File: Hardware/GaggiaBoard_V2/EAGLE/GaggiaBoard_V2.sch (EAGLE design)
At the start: 113 parts, among them IC1 LD117AS33TR, J1 4PIN, J11 PIN262409-1, J12 PIN262409-1, J13 PIN262409-1, J14 PIN262409-1, J15 PIN262409-1, J16 PIN262409-1, J17 PIN262409-1, J18 PIN262409-1, J19 PIN262409-1, J2 Vertical Qwiic Connector, J20 PIN262409-1, J3 Vertical Qwiic Connector, J5 2PIN, J6 3PIN, J7 3PIN, J8 5PIN, J9 3PIN, K1 RELAY-SPDT-JZC-11F, K2 RELAY-SPDT-JZC-11F, K3 AQH213, Q1 600mA/40V, Q10 600mA/40V, Q11 MOSFET_PCH_DUAL-DMP2240UDM, Q2 600mA/40V, Q3 600mA/40V, Q4 600mA/40V, Q5 600mA/40V, Q6 600mA/40V, Q8 600mA/40V, Q9 600mA/40V, U1 BLACKPILL, U2 MAX31855K, U5 TXS0102

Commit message: snubbers
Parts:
- added C16: 10nF, rcl:C-USC1206
- added R35: 220, rcl:R-US_R2512
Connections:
- removed net N$32: C5.1, R13.2
- new net N$27: C5.2, R13.1
- new net N$31: C16.2, R35.1
- net 3WAY: now also R35.2
- net AC_N: no longer R13.1
- net AC_P: now also C16.1, C5.1
- net PUMP_P: now also R13.2; no longer C5.2
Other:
- moved on the sheet: C5, R13
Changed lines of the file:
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@@
 <attribute name="LCSC" value="C107696"/>
+</part>
+<part name="C16" library="rcl" library_urn="urn:adsk.eagle:library:334" deviceset="C-US" device="C1206" package3d_urn="urn:adsk.eagle:package:23618/2" value="10nF">
+<spice>
+<pinmapping spiceprefix="C">
+<pinmap gate="G$1" pin="1" pinorder="1"/>
+<pinmap gate="G$1" pin="2" pinorder="2"/>
+</pinmapping>
+</spice>
+<attribute name="LCSC" value="C107192"/>
+</part>
+<part name="R35" library="rcl" library_urn="urn:adsk.eagle:library:334" deviceset="R-US_" device="R2512" package3d_urn="urn:adsk.eagle:package:23545/2" value="220">
+<spice>
+<pinmapping spiceprefix="R">
+<pinmap gate="G$1" pin="1" pinorder="1"/>
+<pinmap gate="G$1" pin="2" pinorder="2"/>
+</pinmapping>
+</spice>
+<attribute name="LCSC" value="C877859"/>
 </part>
 </parts>
@@
 <instance part="MARK4" gate="G$1" x="243.84" y="40.64" smashed="yes"/>
 <instance part="MARK3" gate="G$1" x="241.3" y="40.64" smashed="yes"/>
-<instance part="R13" gate="G$1" x="205.74" y="165.1" smashed="yes">
-<attribute name="NAME" x="201.93" y="166.5986" size="1.778" layer="95"/>
-<attribute name="VALUE" x="201.93" y="161.798" size="1.778" layer="96"/>
-<attribute name="LCSC" x="205.74" y="165.1" size="1.778" layer="96" display="off"/>
-</instance>
-<instance part="C5" gate="G$1" x="215.9" y="165.1" smashed="yes" rot="R90">
-<attribute name="NAME" x="215.265" y="166.116" size="1.778" layer="95" rot="R90"/>
-<attribute name="VALUE" x="220.091" y="166.116" size="1.778" layer="96" rot="R90"/>
-<attribute name="LCSC" x="215.9" y="165.1" size="1.778" layer="96" rot="R90" display="off"/>
+<instance part="R13" gate="G$1" x="215.9" y="165.1" smashed="yes">
+<attribute name="NAME" x="212.09" y="166.5986" size="1.778" layer="95"/>
+<attribute name="VALUE" x="212.09" y="161.798" size="1.778" layer="96"/>
+<attribute name="LCSC" x="215.9" y="165.1" size="1.778" layer="96" display="off"/>
+</instance>
+<instance part="C5" gate="G$1" x="203.2" y="165.1" smashed="yes" rot="R90">
+<attribute name="NAME" x="202.565" y="166.116" size="1.778" layer="95" rot="R90"/>
+<attribute name="VALUE" x="207.391" y="166.116" size="1.778" layer="96" rot="R90"/>
+<attribute name="LCSC" x="203.2" y="165.1" size="1.778" layer="96" rot="R90" display="off"/>
 </instance>
 <instance part="Q8" gate="G$1" x="40.64" y="101.6" smashed="yes">
@@
 <attribute name="LCSC" x="185.42" y="137.16" size="1.778" layer="96" display="off"/>
 </instance>
+<instance part="C16" gate="G$1" x="203.2" y="147.32" smashed="yes" rot="R90">
+<attribute name="NAME" x="202.565" y="148.336" size="1.778" layer="95" rot="R90"/>
+<attribute name="VALUE" x="207.391" y="148.336" size="1.778" layer="96" rot="R90"/>
+<attribute name="LCSC" x="203.2" y="147.32" size="1.778" layer="96" rot="R90" display="off"/>
+</instance>
+<instance part="R35" gate="G$1" x="215.9" y="147.32" smashed="yes">
+<attribute name="NAME" x="212.09" y="148.8186" size="1.778" layer="95"/>
+<attribute name="VALUE" x="212.09" y="144.018" size="1.778" layer="96"/>
+<attribute name="LCSC" x="215.9" y="147.32" size="1.778" layer="96" display="off"/>
+</instance>
 </instances>
 <busses>
@@
 </segment>
 <segment>
-<label x="187.96" y="170.18" size="1.778" layer="95"/>
+<label x="210.82" y="170.18" size="1.778" layer="95"/>
 <pinref part="J18" gate="-1" pin="1"/>
-<pinref part="R13" gate="G$1" pin="1"/>
-<wire x1="198.12" y1="170.18" x2="226.06" y2="170.18" width="0.1524" layer="91"/>
-<wire x1="200.66" y1="165.1" x2="198.12" y2="165.1" width="0.1524" layer="91"/>
-<wire x1="198.12" y1="165.1" x2="198.12" y2="170.18" width="0.1524" layer="91"/>
-<junction x="198.12" y="170.18"/>
-<wire x1="187.96" y1="170.18" x2="198.12" y2="170.18" width="0.1524" layer="91"/>
+<wire x1="210.82" y1="170.18" x2="226.06" y2="170.18" width="0.1524" layer="91"/>
 </segment>
 <segment>
@@
 <label x="30.48" y="27.94" size="1.778" layer="95"/>
 </segment>
+<segment>
+<pinref part="C5" gate="G$1" pin="1"/>
+<wire x1="200.66" y1="165.1" x2="195.58" y2="165.1" width="0.1524" layer="91"/>
+<label x="195.58" y="165.1" size="1.778" layer="95"/>
+</segment>
+<segment>
+<pinref part="C16" gate="G$1" pin="1"/>
+<wire x1="200.66" y1="147.32" x2="195.58" y2="147.32" width="0.1524" layer="91"/>
+<label x="195.58" y="147.32" size="1.778" layer="95"/>
+</segment>
 </net>
 <net name="HEATER_2" class="0">
@@
 <net name="3WAY" class="0">
 <segment>
-<wire x1="226.06" y1="139.7" x2="218.44" y2="139.7" width="0.1524" layer="91"/>
 <pinref part="J16" gate="-1" pin="1"/>
 <pinref part="K3" gate="G$1" pin="DS1"/>
+<wire x1="226.06" y1="139.7" x2="223.52" y2="139.7" width="0.1524" layer="91"/>
+<pinref part="R35" gate="G$1" pin="2"/>
+<wire x1="223.52" y1="139.7" x2="218.44" y2="139.7" width="0.1524" layer="91"/>
+<wire x1="220.98" y1="147.32" x2="223.52" y2="147.32" width="0.1524" layer="91"/>
+<wire x1="223.52" y1="147.32" x2="223.52" y2="139.7" width="0.1524" layer="91"/>
+<junction x="223.52" y="139.7"/>
 </segment>
 </net>
@@
 </segment>
 </net>
-<net name="N$32" class="0">
-<segment>
-<pinref part="C5" gate="G$1" pin="1"/>
-<pinref part="R13" gate="G$1" pin="2"/>
-<wire x1="213.36" y1="165.1" x2="210.82" y2="165.1" width="0.1524" layer="91"/>
-</segment>
-</net>
 <net name="N$33" class="0">
 <segment>
@@
 <pinref part="J17" gate="-1" pin="1"/>
 <wire x1="226.06" y1="160.02" x2="223.52" y2="160.02" width="0.1524" layer="91"/>
+<pinref part="TR1" gate="G$1" pin="A1"/>
 <wire x1="223.52" y1="160.02" x2="170.18" y2="160.02" width="0.1524" layer="91"/>
-<pinref part="C5" gate="G$1" pin="2"/>
+<wire x1="170.18" y1="160.02" x2="170.18" y2="162.56" width="0.1524" layer="91"/>
+<pinref part="R13" gate="G$1" pin="2"/>
 <wire x1="220.98" y1="165.1" x2="223.52" y2="165.1" width="0.1524" layer="91"/>
 <wire x1="223.52" y1="165.1" x2="223.52" y2="160.02" width="0.1524" layer="91"/>
 <junction x="223.52" y="160.02"/>
-<pinref part="TR1" gate="G$1" pin="A1"/>
-<wire x1="170.18" y1="160.02" x2="170.18" y2="162.56" width="0.1524" layer="91"/>
 </segment>
 </net>
@@
 </segment>
 </net>
+<net name="N$27" class="0">
+<segment>
+<pinref part="C5" gate="G$1" pin="2"/>
+<pinref part="R13" gate="G$1" pin="1"/>
+<wire x1="208.28" y1="165.1" x2="210.82" y2="165.1" width="0.1524" layer="91"/>
+</segment>
+</net>
+<net name="N$31" class="0">
+<segment>
+<pinref part="C16" gate="G$1" pin="2"/>
+<pinref part="R35" gate="G$1" pin="1"/>
+<wire x1="208.28" y1="147.32" x2="210.82" y2="147.32" width="0.1524" layer="91"/>
+</segment>
+</net>

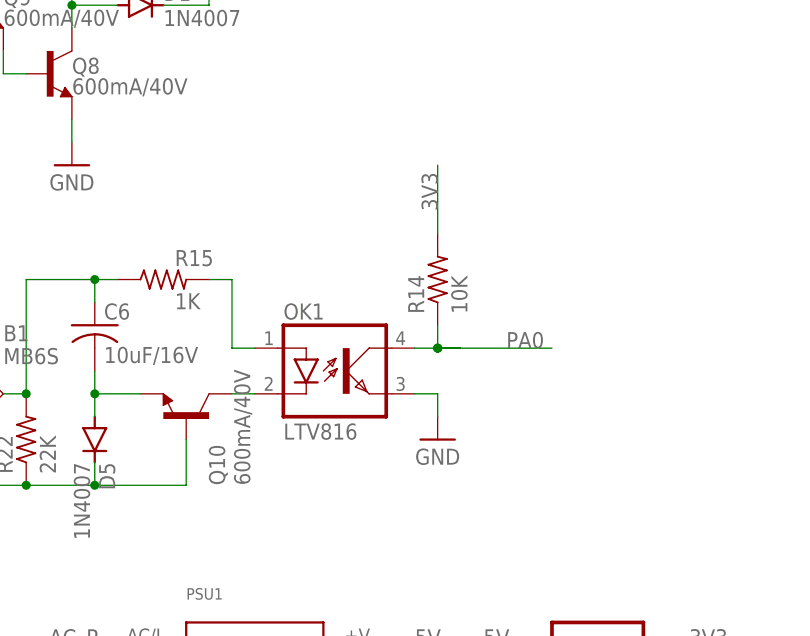
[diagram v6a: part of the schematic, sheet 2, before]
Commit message: OK1 part change
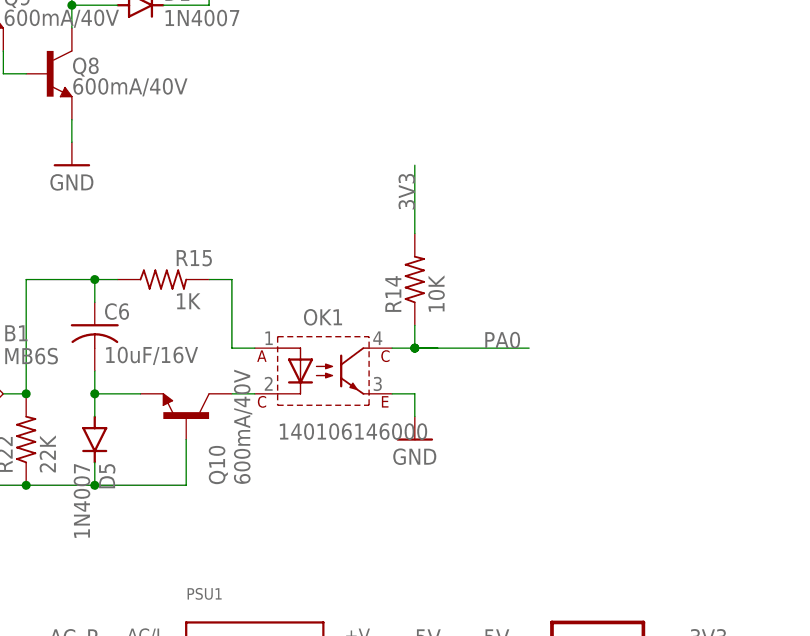
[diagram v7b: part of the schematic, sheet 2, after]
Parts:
- OK1: value LTV816 -> 140106146000; device optocoupler:LTV816 -> Wurth_Optocoupler_WL-OCPT:WL-OCPT_SERIES_101X_140106146000; LCSC C2944043 -> C141610
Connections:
- net GND: now also OK1.3; no longer OK1.EMIT
- net N$44: now also OK1.1; no longer OK1.A
- net N$7: now also OK1.2; no longer OK1.C
- net PA0: now also OK1.4; no longer OK1.COL
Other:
- moved on the sheet: OK1, R14
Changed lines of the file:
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@@
 <part name="FRAME1" library="frames" library_urn="urn:adsk.eagle:library:229" deviceset="LETTER_L" device=""/>
 <part name="FRAME2" library="frames" library_urn="urn:adsk.eagle:library:229" deviceset="LETTER_L" device=""/>
-<part name="OK1" library="optocoupler" library_urn="urn:adsk.eagle:library:320" deviceset="LTV816" device="" package3d_urn="urn:adsk.eagle:package:21938/1" override_package3d_urn="urn:adsk.eagle:package:36461858/2" override_package_urn="urn:adsk.eagle:footprint:21858/1">
-<attribute name="LCSC" value="C2944043"/>
-</part>
 <part name="OK2" library="discrete" library_urn="urn:adsk.eagle:library:211" deviceset="MOC3021M" device="DIL06O" override_package3d_urn="urn:adsk.eagle:package:36461862/2" override_package_urn="urn:adsk.eagle:footprint:36461863/1">
 <attribute name="LCSC" value="C5242"/>
@@
 </spice>
 <attribute name="LCSC" value="C877859"/>
+</part>
+<part name="OK1" library="Wurth_Optocoupler_WL-OCPT" library_urn="urn:adsk.eagle:library:20377805" deviceset="WL-OCPT_SERIES_101X" device="" package3d_urn="urn:adsk.eagle:package:25398557/3" technology="_140106146000" value="140106146000">
+<attribute name="LCSC" value="C141610"/>
 </part>
 </parts>
@@
 <attribute name="VALUE" x="15.24" y="132.715" size="1.778" layer="96" align="center"/>
 </instance>
-<instance part="OK1" gate="G$1" x="73.66" y="68.58" smashed="yes">
-<attribute name="NAME" x="66.675" y="74.295" size="1.778" layer="95"/>
-<attribute name="VALUE" x="66.675" y="60.96" size="1.778" layer="96"/>
-<attribute name="LCSC" x="73.66" y="68.58" size="1.778" layer="96" display="off"/>
-</instance>
 <instance part="R20" gate="G$1" x="20.32" y="76.2" smashed="yes">
 <attribute name="NAME" x="16.51" y="77.6986" size="1.778" layer="95"/>
@@
 <attribute name="LCSC" x="20.32" y="76.2" size="1.778" layer="96" display="off"/>
 </instance>
-<instance part="SUPPLY8" gate="G$1" x="83.82" y="60.96" smashed="yes">
-<attribute name="VALUE" x="83.82" y="59.055" size="1.778" layer="96" align="center"/>
-</instance>
-<instance part="R14" gate="G$1" x="83.82" y="78.74" smashed="yes" rot="R90">
-<attribute name="NAME" x="82.3214" y="74.93" size="1.778" layer="95" rot="R90"/>
-<attribute name="VALUE" x="87.122" y="74.93" size="1.778" layer="96" rot="R90"/>
-<attribute name="LCSC" x="83.82" y="78.74" size="1.778" layer="96" rot="R90" display="off"/>
+<instance part="SUPPLY8" gate="G$1" x="81.28" y="60.96" smashed="yes">
+<attribute name="VALUE" x="81.28" y="59.055" size="1.778" layer="96" align="center"/>
+</instance>
+<instance part="R14" gate="G$1" x="81.28" y="78.74" smashed="yes" rot="R90">
+<attribute name="NAME" x="79.7814" y="74.93" size="1.778" layer="95" rot="R90"/>
+<attribute name="VALUE" x="84.582" y="74.93" size="1.778" layer="96" rot="R90"/>
+<attribute name="LCSC" x="81.28" y="78.74" size="1.778" layer="96" rot="R90" display="off"/>
 </instance>
 <instance part="B1" gate="G$1" x="30.48" y="66.04" smashed="yes" rot="MR180">
@@
 <attribute name="VALUE" x="212.09" y="144.018" size="1.778" layer="96"/>
 <attribute name="LCSC" x="215.9" y="147.32" size="1.778" layer="96" display="off"/>
+</instance>
+<instance part="OK1" gate="G$1" x="71.12" y="68.58" smashed="yes">
+<attribute name="NAME" x="71.12" y="73.66" size="1.778" layer="95" align="bottom-center"/>
+<attribute name="VALUE" x="66.04" y="60.96" size="1.778" layer="96"/>
+<attribute name="LCSC" x="71.12" y="68.58" size="1.778" layer="96" display="off"/>
 </instance>
 </instances>
@@
 </segment>
 <segment>
-<pinref part="OK1" gate="G$1" pin="EMIT"/>
 <pinref part="SUPPLY8" gate="G$1" pin="GND"/>
-<wire x1="81.28" y1="66.04" x2="83.82" y2="66.04" width="0.1524" layer="91"/>
-<wire x1="83.82" y1="66.04" x2="83.82" y2="63.5" width="0.1524" layer="91"/>
+<wire x1="78.74" y1="66.04" x2="81.28" y2="66.04" width="0.1524" layer="91"/>
+<wire x1="81.28" y1="66.04" x2="81.28" y2="63.5" width="0.1524" layer="91"/>
+<pinref part="OK1" gate="G$1" pin="3"/>
 </segment>
 <segment>
@@
 <segment>
 <pinref part="R14" gate="G$1" pin="2"/>
-<wire x1="83.82" y1="83.82" x2="83.82" y2="91.44" width="0.1524" layer="91"/>
-<label x="83.82" y="86.36" size="1.778" layer="95" rot="R90"/>
+<wire x1="81.28" y1="83.82" x2="81.28" y2="91.44" width="0.1524" layer="91"/>
+<label x="81.28" y="86.36" size="1.778" layer="95" rot="R90"/>
 </segment>
 <segment>
@@
 <net name="PA0" class="0">
 <segment>
-<wire x1="83.82" y1="71.12" x2="96.52" y2="71.12" width="0.1524" layer="91"/>
-<junction x="83.82" y="71.12"/>
-<label x="91.44" y="71.12" size="1.778" layer="95"/>
-<pinref part="OK1" gate="G$1" pin="COL"/>
+<wire x1="81.28" y1="71.12" x2="93.98" y2="71.12" width="0.1524" layer="91"/>
+<junction x="81.28" y="71.12"/>
+<label x="88.9" y="71.12" size="1.778" layer="95"/>
+<wire x1="78.74" y1="71.12" x2="81.28" y2="71.12" width="0.1524" layer="91"/>
+<pinref part="R14" gate="G$1" pin="1"/>
 <wire x1="81.28" y1="71.12" x2="83.82" y2="71.12" width="0.1524" layer="91"/>
-<pinref part="R14" gate="G$1" pin="1"/>
-<wire x1="83.82" y1="71.12" x2="86.36" y2="71.12" width="0.1524" layer="91"/>
-<wire x1="83.82" y1="73.66" x2="83.82" y2="71.12" width="0.1524" layer="91"/>
-<junction x="83.82" y="71.12"/>
+<wire x1="81.28" y1="73.66" x2="81.28" y2="71.12" width="0.1524" layer="91"/>
+<junction x="81.28" y="71.12"/>
+<pinref part="OK1" gate="G$1" pin="4"/>
 </segment>
 </net>
@@
 <segment>
 <pinref part="Q10" gate="G$1" pin="C"/>
-<pinref part="OK1" gate="G$1" pin="C"/>
 <wire x1="60.96" y1="66.04" x2="63.5" y2="66.04" width="0.1524" layer="91"/>
+<pinref part="OK1" gate="G$1" pin="2"/>
 </segment>
 </net>
@@
 <wire x1="58.42" y1="78.74" x2="60.96" y2="78.74" width="0.1524" layer="91"/>
 <wire x1="60.96" y1="78.74" x2="60.96" y2="71.12" width="0.1524" layer="91"/>
-<pinref part="OK1" gate="G$1" pin="A"/>
 <wire x1="60.96" y1="71.12" x2="63.5" y2="71.12" width="0.1524" layer="91"/>
-</segment>
-</net>
+<pinref part="OK1" gate="G$1" pin="1"/>
+</segment>
+</net>
